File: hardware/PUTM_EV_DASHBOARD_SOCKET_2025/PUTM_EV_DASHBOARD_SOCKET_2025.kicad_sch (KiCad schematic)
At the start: 0 parts

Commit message: jest jako tako
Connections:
- no-connect marks 0 -> 46
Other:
- sheet BUTTONS ports: added BUTTON_1, BUTTON_2, BUTTON_3, BUTTON_4, BUTTON_5; removed none
- sheet CAN ports: added CAN_GND, CAN_N, CAN_P, CAN_VDD; removed none
- sheet LEDS ports: added AMS, FUSE_LED, SAFETY_LED; removed none
- sheet POWER ports: added OUT_3_3_V, OUT_5_V, POWER1, POWER_EN; removed none
- sheet SOCKETS_2X20 ports: added 5V, AMS, BUTTON_1, BUTTON_2, BUTTON_3, BUTTON_4, BUTTON_5, FUSE_LED, P10, P14, P15, PA10, PA11, PA12, PA15, PA3, PA4, PA5, PA6, PA7, PA8, PB0, PB1, PB10, PB15, PB2, PB5, PB6, PB7, PC7, PE40, PG10, PG2, PG3, PG4, PG9, PH11, PH4, PH5, SAFETY_LED, VCC; removed none
- sheet SWD ports: added SWD_RST, SWD_SWO, SWD_SW_CLK, SWD_SW_DIO, SWD_VCC_+3.3V; removed none

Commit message: gotowe
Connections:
- no-connect marks 46 -> 45
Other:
- sheet POWER ports: added none; removed POWER_EN
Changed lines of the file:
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@@
-	)
-	(no_connect
-		(at 256.54 128.27)
 	)
 	(no_connect
@@
 			(effects
 				(font
-					(size 1.27 1.27)
-				)
-				(justify left)
-			)
-		)
-		(pin "POWER_EN" input
-			(at 256.54 128.27 180)
-			(effects
-				(font

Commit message: g2
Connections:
- no-connect marks 45 -> 44
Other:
- sheet SWD ports: added none; removed SWD_SWO
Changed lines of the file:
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@@
-	)
-	(no_connect
-		(at 128.27 19.05)
 	)
 	(no_connect
@@
 			(effects
 				(font
-					(size 1.27 1.27)
-				)
-				(justify right)
-			)
-		)
-		(pin "SWD_SWO" input
-			(at 128.27 19.05 90)
-			(effects
-				(font

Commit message: g3
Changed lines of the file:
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@@
 	)
 	(no_connect
-		(at 125.73 19.05)
+		(at 120.65 17.78)
 	)
 	(no_connect
@@
 	)
 	(no_connect
-		(at 86.36 17.78)
+		(at 76.2 17.78)
 	)
 	(no_connect
@@
 	)
 	(no_connect
-		(at 90.17 17.78)
+		(at 80.01 17.78)
 	)
 	(no_connect
@@
 	)
 	(no_connect
-		(at 92.71 17.78)
+		(at 82.55 17.78)
 	)
 	(no_connect
@@
 	)
 	(no_connect
-		(at 95.25 17.78)
+		(at 85.09 17.78)
 	)
 	(no_connect
@@
 	)
 	(no_connect
-		(at 130.81 19.05)
+		(at 125.73 17.78)
 	)
 	(no_connect
@@
 	)
 	(no_connect
-		(at 133.35 19.05)
+		(at 128.27 17.78)
 	)
 	(no_connect
@@
 	)
 	(no_connect
-		(at 135.89 19.05)
+		(at 130.81 17.78)
 	)
 	(bus_entry
@@
 	)
 	(bus_entry
-		(at 77.47 43.18)
+		(at 64.77 43.18)
 		(size -2.54 2.54)
 		(stroke
@@
 	)
 	(bus_entry
-		(at 162.56 33.655)
+		(at 162.56 34.29)
 		(size 2.54 -2.54)
 		(stroke
@@
 	)
 	(bus_entry
-		(at 77.47 49.53)
+		(at 64.77 49.53)
 		(size -2.54 2.54)
 		(stroke
@@
 	)
 	(bus_entry
-		(at 77.47 36.83)
+		(at 64.77 36.83)
 		(size -2.54 -2.54)
 		(stroke
@@
 	(wire
 		(pts
-			(xy 74.93 35.56) (xy 73.66 35.56)
-		)
-		(stroke
-			(width 0)
-			(type default)
-		)
-	)
-	(bus
-		(pts
-			(xy 77.47 97.79) (xy 157.48 97.79)
+			(xy 62.23 49.53) (xy 60.96 49.53)
 		)
 		(stroke
@@
 	(wire
 		(pts
-			(xy 74.93 45.72) (xy 74.93 43.18)
+			(xy 62.23 45.72) (xy 62.23 43.18)
 		)
 		(stroke
@@
 	(wire
 		(pts
-			(xy 74.93 52.07) (xy 74.93 49.53)
+			(xy 62.23 52.07) (xy 62.23 49.53)
 		)
 		(stroke
@@
 		)
 	)
+	(bus
+		(pts
+			(xy 64.77 97.79) (xy 157.48 97.79)
+		)
+		(stroke
+			(width 0)
+			(type default)
+		)
+	)
 	(wire
 		(pts
@@
 	(bus
 		(pts
-			(xy 77.47 35.56) (xy 77.47 36.83)
+			(xy 64.77 35.56) (xy 64.77 36.83)
 		)
 		(stroke
@@
 		)
 	)
-	(wire
-		(pts
-			(xy 74.93 43.18) (xy 73.66 43.18)
-		)
-		(stroke
-			(width 0)
-			(type default)
-		)
-	)
 	(bus
 		(pts
@@
 	(bus
 		(pts
-			(xy 77.47 43.18) (xy 77.47 49.53)
-		)
-		(stroke
-			(width 0)
-			(type default)
-		)
-	)
-	(bus
-		(pts
-			(xy 77.47 49.53) (xy 77.47 97.79)
+			(xy 64.77 43.18) (xy 64.77 49.53)
+		)
+		(stroke
+			(width 0)
+			(type default)
+		)
+	)
+	(bus
+		(pts
+			(xy 64.77 49.53) (xy 64.77 97.79)
 		)
 		(stroke
@@
 	(bus
 		(pts
-			(xy 162.56 33.655) (xy 162.56 36.83)
-		)
-		(stroke
-			(width 0)
-			(type default)
-		)
-	)
-	(wire
-		(pts
-			(xy 165.1 31.115) (xy 165.1 31.75)
+			(xy 162.56 34.29) (xy 162.56 36.83)
 		)
 		(stroke
@@
 		)
 	)
+	(wire
+		(pts
+			(xy 62.23 43.18) (xy 60.96 43.18)
+		)
+		(stroke
+			(width 0)
+			(type default)
+		)
+	)
 	(bus
 		(pts
@@
 	(bus
 		(pts
-			(xy 162.56 33.02) (xy 162.56 33.655)
+			(xy 162.56 33.02) (xy 162.56 34.29)
 		)
 		(stroke
@@
 	(bus
 		(pts
-			(xy 77.47 36.83) (xy 77.47 43.18)
+			(xy 64.77 36.83) (xy 64.77 43.18)
 		)
 		(stroke
@@
 		)
 	)
-	(wire
-		(pts
-			(xy 74.93 49.53) (xy 73.66 49.53)
-		)
-		(stroke
-			(width 0)
-			(type default)
-		)
-	)
 	(bus
 		(pts
@@
 	(wire
 		(pts
+			(xy 62.23 35.56) (xy 60.96 35.56)
+		)
+		(stroke
+			(width 0)
+			(type default)
+		)
+	)
+	(wire
+		(pts
 			(xy 160.02 26.67) (xy 160.02 24.13)
 		)
@@
 	(wire
 		(pts
-			(xy 74.93 34.29) (xy 74.93 35.56)
+			(xy 62.23 34.29) (xy 62.23 35.56)
 		)
 		(stroke
@@
 	)
 	(label "LED_2"
-		(at 73.66 43.18 0)
+		(at 62.23 43.18 0)
 		(effects
 			(font
@@
 	)
 	(label "LED_3"
-		(at 73.66 49.53 0)
+		(at 62.23 49.53 0)
 		(effects
 			(font
@@
 	)
 	(label "LED_1"
-		(at 73.66 35.56 0)
+		(at 62.23 35.56 0)
 		(effects
 			(font
@@
 	)
 	(sheet
-		(at 24.13 83.185)
+		(at 24.13 83.82)
 		(size 25.4 77.47)
 		(exclude_from_sim no)
@@
 		)
 		(property "Sheetname" "BUTTONS"
-			(at 24.13 82.55 0)
+			(at 24.13 83.185 0)
 			(effects
 				(font
@@
 		)
 		(property "Sheetfile" "BUTTONS.kicad_sch"
-			(at 24.13 161.2396 0)
+			(at 24.13 161.8746 0)
 			(effects
 				(font
@@
 	)
 	(sheet
-		(at 46.99 26.67)
+		(at 34.29 26.67)
 		(size 26.67 33.02)
 		(exclude_from_sim no)
@@
 		)
 		(property "Sheetname" "LEDS"
-			(at 46.99 25.9584 0)
+			(at 34.29 25.9584 0)
 			(effects
 				(font
@@
 		)
 		(property "Sheetfile" "LEDS.kicad_sch"
-			(at 46.99 60.2746 0)
+			(at 34.29 60.2746 0)
 			(effects
 				(font
@@
 		)
 		(pin "AMS" input
-			(at 73.66 35.56 0)
+			(at 60.96 35.56 0)
 			(effects
 				(font
@@
 		)
 		(pin "FUSE_LED" input
-			(at 73.66 43.18 0)
+			(at 60.96 43.18 0)
 			(effects
 				(font
@@
 		)
 		(pin "SAFETY_LED" input
-			(at 73.66 49.53 0)
+			(at 60.96 49.53 0)
 			(effects
 				(font
@@
 	)
 	(sheet
-		(at 120.65 19.05)
+		(at 115.57 17.78)
 		(size 35.56 69.85)
 		(exclude_from_sim no)
@@
 		)
 		(property "Sheetname" "SWD"
-			(at 120.65 18.3384 0)
+			(at 115.57 17.0684 0)
 			(effects
 				(font
@@
 		)
 		(property "Sheetfile" "SWD.kicad_sch"
-			(at 120.65 89.4846 0)
+			(at 115.57 88.2146 0)
 			(effects
 				(font
@@
 		)
 		(pin "SWD_RST" input
-			(at 125.73 19.05 90)
+			(at 120.65 17.78 90)
 			(effects
 				(font
@@
 		)
 		(pin "SWD_SW_CLK" input
-			(at 130.81 19.05 90)
+			(at 125.73 17.78 90)
 			(effects
 				(font
@@
 		)
 		(pin "SWD_SW_DIO" input
-			(at 133.35 19.05 90)
+			(at 128.27 17.78 90)
 			(effects
 				(font
@@
 		)
 		(pin "SWD_VCC_+3.3V" input
-			(at 135.89 19.05 90)
+			(at 130.81 17.78 90)
 			(effects
 				(font
@@
 	)
 	(sheet
-		(at 80.01 17.78)
+		(at 69.85 17.78)
 		(size 38.1 53.34)
 		(exclude_from_sim no)
@@
 		)
 		(property "Sheetname" "CAN"
-			(at 80.01 17.0684 0)
+			(at 69.85 17.0684 0)
 			(effects
 				(font
@@
 		)
 		(property "Sheetfile" "CAN.kicad_sch"
-			(at 80.01 71.7046 0)
+			(at 69.85 71.7046 0)
 			(effects
 				(font
@@
 		)
 		(pin "CAN_GND" input
-			(at 86.36 17.78 90)
+			(at 76.2 17.78 90)
 			(effects
 				(font
@@
 		)
 		(pin "CAN_N" input
-			(at 90.17 17.78 90)
+			(at 80.01 17.78 90)
 			(effects
 				(font
@@
 		)
 		(pin "CAN_P" input
-			(at 92.71 17.78 90)
+			(at 82.55 17.78 90)
 			(effects
 				(font
@@
 		)
 		(pin "CAN_VDD" input
-			(at 95.25 17.78 90)
-			(effects
-				(font
+			(at 85.09 17.78 90)
+			(effects
+				(font

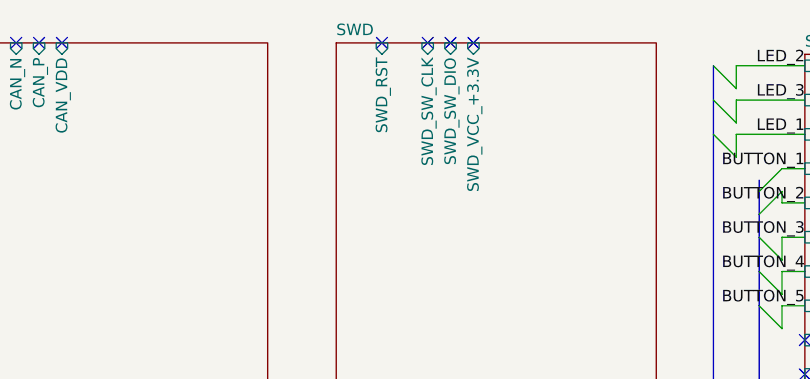
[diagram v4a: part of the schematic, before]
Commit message: poprawione opisy i złącze swd, gnazdo POWER jest na krawędzi płytki
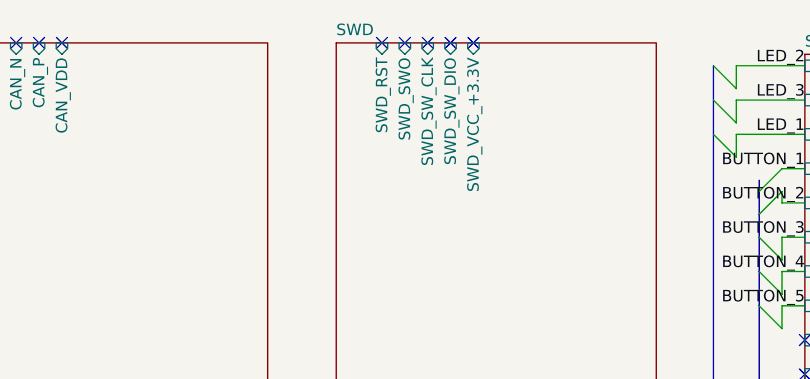
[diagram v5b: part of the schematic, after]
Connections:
- no-connect marks 44 -> 45
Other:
- sheet SWD ports: added SWD_SWO; removed none
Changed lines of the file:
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@@
+	)
+	(no_connect
+		(at 123.19 17.78)
 	)
 	(no_connect
@@
 			(effects
 				(font
+					(size 1.27 1.27)
+				)
+				(justify right)
+			)
+		)
+		(pin "SWD_SWO" input
+			(at 123.19 17.78 90)
+			(effects
+				(font

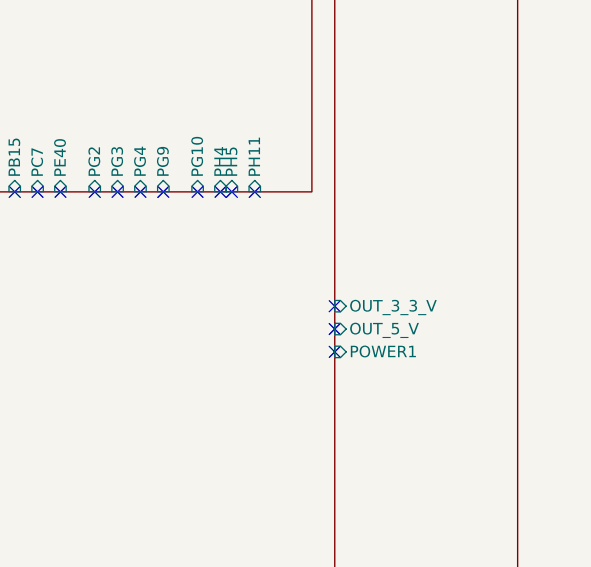
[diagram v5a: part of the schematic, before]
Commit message: dodano łezki do pól smd, pola lutownicze do przelotek, dodano zabezpieczenie przed odwrotna polaryzacją, odsunięto ścieżki od krawędzi płytki, poprawiono can,
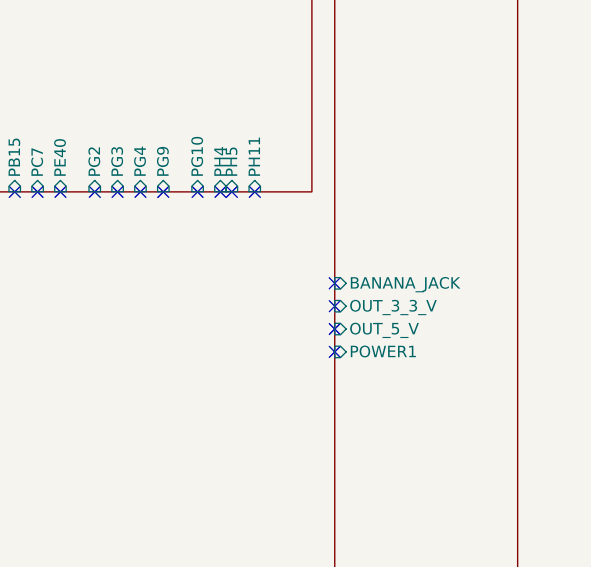
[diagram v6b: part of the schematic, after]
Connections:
- no-connect marks 45 -> 46
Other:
- sheet POWER ports: added BANANA_JACK; removed none
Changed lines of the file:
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@@
+	)
+	(no_connect
+		(at 256.54 118.11)
 	)
 	(no_connect
@@
 			(effects
 				(font
+					(size 1.27 1.27)
+				)
+				(justify left)
+			)
+		)
+		(pin "BANANA_JACK" input
+			(at 256.54 118.11 180)
+			(effects
+				(font
